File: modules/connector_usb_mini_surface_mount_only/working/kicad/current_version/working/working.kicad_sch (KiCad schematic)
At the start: 1 part, among them J1 scumnsmo

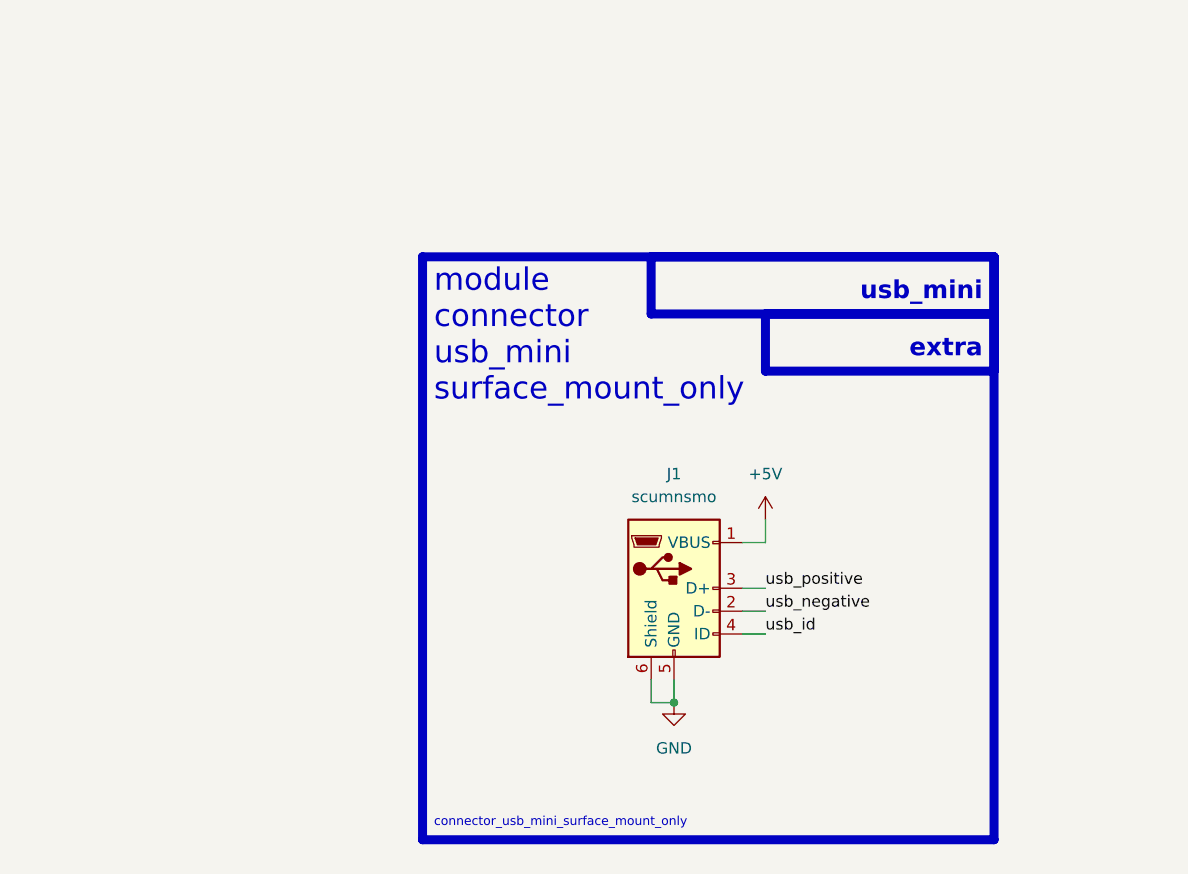
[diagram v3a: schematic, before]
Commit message: schematic formatting
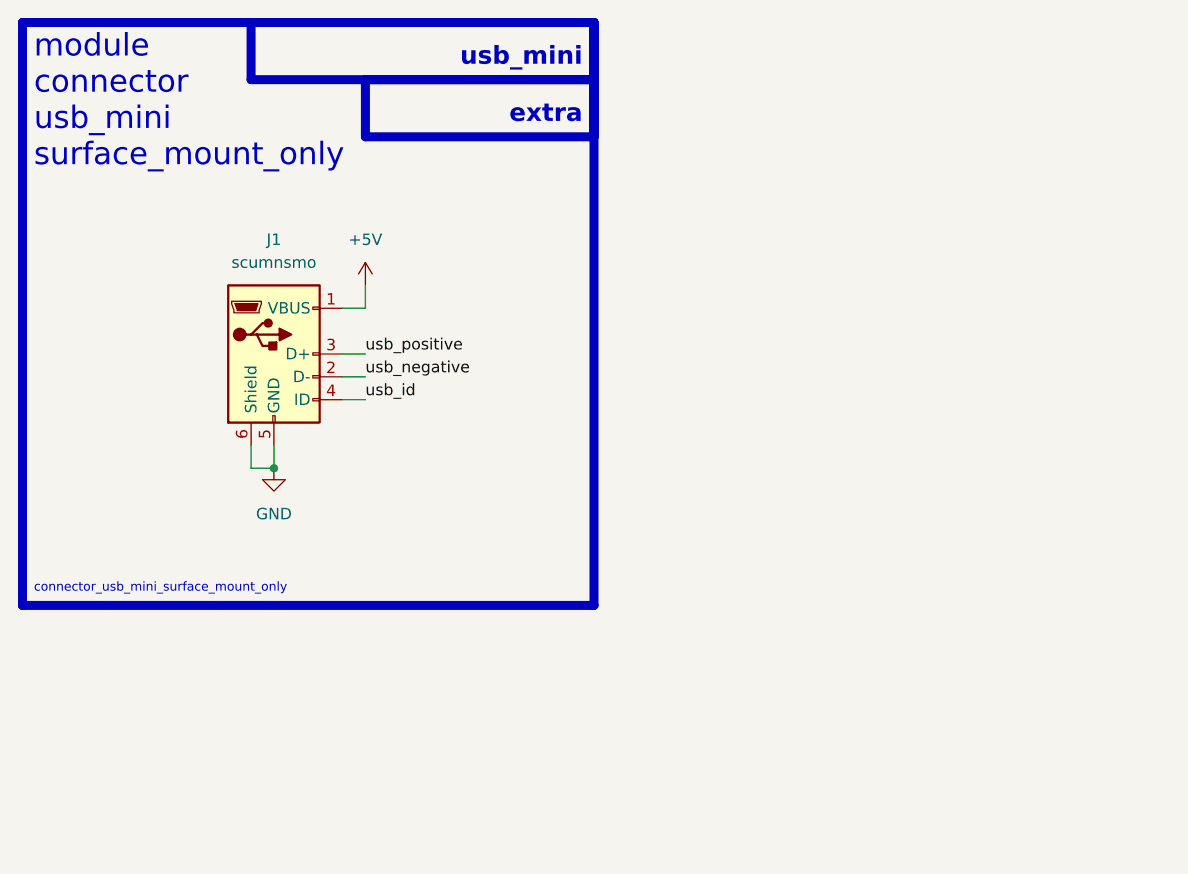
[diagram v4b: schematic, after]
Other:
- moved on the sheet: J1
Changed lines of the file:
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@@
 (kicad_sch (version 20230121) (generator eeschema)
-  (paper "A4")
-  (junction (at 146.05 110.49) (diameter 0) (color 0 0 0 0)
+  (paper "A5")
+  (junction (at 101.6 84.455) (diameter 0) (color 0 0 0 0)
   )
-  (wire (pts (xy 153.67 102.87) (xy 156.21 102.87))
+  (wire (pts (xy 109.22 76.835) (xy 111.76 76.835))
     (stroke (width 0) (type default))
   )
-  (wire (pts (xy 146.05 107.95) (xy 146.05 110.49))
+  (wire (pts (xy 101.6 81.915) (xy 101.6 84.455))
     (stroke (width 0) (type default))
   )
-  (wire (pts (xy 156.21 90.17) (xy 156.21 92.71))
+  (wire (pts (xy 111.76 64.135) (xy 111.76 66.675))
     (stroke (width 0) (type default))
   )
-  (wire (pts (xy 153.67 97.79) (xy 156.21 97.79))
+  (wire (pts (xy 109.22 71.755) (xy 111.76 71.755))
     (stroke (width 0) (type default))
   )
-  (wire (pts (xy 143.51 110.49) (xy 146.05 110.49))
+  (wire (pts (xy 99.06 84.455) (xy 101.6 84.455))
     (stroke (width 0) (type default))
   )
-  (wire (pts (xy 153.67 92.71) (xy 156.21 92.71))
+  (wire (pts (xy 109.22 66.675) (xy 111.76 66.675))
     (stroke (width 0) (type default))
   )
-  (wire (pts (xy 143.51 107.95) (xy 143.51 110.49))
+  (wire (pts (xy 99.06 81.915) (xy 99.06 84.455))
     (stroke (width 0) (type default))
   )
-  (wire (pts (xy 153.67 100.33) (xy 156.21 100.33))
+  (wire (pts (xy 109.22 74.295) (xy 111.76 74.295))
     (stroke (width 0) (type default))
   )
-  (rectangle (start 118.11 60.96) (end 181.61 125.73)
+  (rectangle (start 73.66 34.925) (end 137.16 99.695)
     (stroke (width 1) (type default))
     (fill (type none))
   )
-  (rectangle (start 156.21 67.31) (end 181.61 73.66)
+  (rectangle (start 111.76 41.275) (end 137.16 47.625)
     (stroke (width 1) (type default))
     (fill (type none))
   )
-  (rectangle (start 143.51 60.96) (end 181.61 67.31)
+  (rectangle (start 99.06 34.925) (end 137.16 41.275)
     (stroke (width 1) (type default))
     (fill (type none))
   )
-  (text "extra" (at 180.34 72.39 0)
+  (text "extra" (at 135.89 46.355 0)
     (effects (font (size 2 2) (thickness 0.8) bold) (justify right bottom))
   )
-  (text "usb_mini" (at 180.34 66.04 0)
+  (text "usb_mini" (at 135.89 40.005 0)
     (effects (font (size 2 2) (thickness 0.8) bold) (justify right bottom))
   )
-  (text "module\nconnector\nusb_mini\nsurface_mount_only\n\n" (at 119.38 81.28 0)
+  (text "module\nconnector\nusb_mini\nsurface_mount_only\n\n" (at 74.93 55.245 0)
     (effects (font (size 2.5 2.5)) (justify left bottom))
   )
-  (text "connector_usb_mini_surface_mount_only" (at 119.38 124.46 0)
+  (text "connector_usb_mini_surface_mount_only" (at 74.93 98.425 0)
     (effects (font (size 1 1)) (justify left bottom))
   )
-  (label "usb_id" (at 156.21 102.87 0) (fields_autoplaced)
+  (label "usb_id" (at 111.76 76.835 0) (fields_autoplaced)
     (effects (font (size 1.27 1.27)) (justify left bottom))
   )
-  (label "usb_positive" (at 156.21 97.79 0) (fields_autoplaced)
+  (label "usb_positive" (at 111.76 71.755 0) (fields_autoplaced)
     (effects (font (size 1.27 1.27)) (justify left bottom))
   )
-  (label "usb_negative" (at 156.21 100.33 0) (fields_autoplaced)
+  (label "usb_negative" (at 111.76 74.295 0) (fields_autoplaced)
     (effects (font (size 1.27 1.27)) (justify left bottom))
   )
-  (symbol (lib_id "power:GND") (at 146.05 110.49 0) (unit 1)
+  (symbol (lib_id "power:GND") (at 101.6 84.455 0) (unit 1)
     (in_bom yes) (on_board yes) (dnp no) (fields_autoplaced)
-    (property "Reference" "#PWR012" (at 146.05 116.84 0)
+    (property "Reference" "#PWR012" (at 101.6 90.805 0)
       (effects (font (size 1.27 1.27)) hide)
     )
-    (property "Value" "GND" (at 146.05 115.57 0)
+    (property "Value" "GND" (at 101.6 89.535 0)
       (effects (font (size 1.27 1.27)))
     )
-    (property "Footprint" "" (at 146.05 110.49 0)
+    (property "Footprint" "" (at 101.6 84.455 0)
       (effects (font (size 1.27 1.27)) hide)
     )
-    (property "Datasheet" "" (at 146.05 110.49 0)
+    (property "Datasheet" "" (at 101.6 84.455 0)
       (effects (font (size 1.27 1.27)) hide)
     )
@@
     )
   )
-  (symbol (lib_id "power:+5V") (at 156.21 90.17 0) (unit 1)
+  (symbol (lib_id "power:+5V") (at 111.76 64.135 0) (unit 1)
     (in_bom yes) (on_board yes) (dnp no) (fields_autoplaced)
-    (property "Reference" "#PWR013" (at 156.21 93.98 0)
+    (property "Reference" "#PWR013" (at 111.76 67.945 0)
       (effects (font (size 1.27 1.27)) hide)
     )
-    (property "Value" "+5V" (at 156.21 85.09 0)
+    (property "Value" "+5V" (at 111.76 59.055 0)
       (effects (font (size 1.27 1.27)))
     )
-    (property "Footprint" "" (at 156.21 90.17 0)
+    (property "Footprint" "" (at 111.76 64.135 0)
       (effects (font (size 1.27 1.27)) hide)
     )
-    (property "Datasheet" "" (at 156.21 90.17 0)
+    (property "Datasheet" "" (at 111.76 64.135 0)
       (effects (font (size 1.27 1.27)) hide)
     )
@@
     )
   )
-  (symbol (lib_id "oomlout_oomp_part_symbols:scumnsmo_electronic_socket_usb_mini_surface_mount_only") (at 146.05 97.79 0) (unit 1)
+  (symbol (lib_id "oomlout_oomp_part_symbols:scumnsmo_electronic_socket_usb_mini_surface_mount_only") (at 101.6 71.755 0) (unit 1)
     (in_bom yes) (on_board yes) (dnp no) (fields_autoplaced)
-    (property "Reference" "J1" (at 146.05 85.09 0)
+    (property "Reference" "J1" (at 101.6 59.055 0)
       (effects (font (size 1.27 1.27)))
     )
-    (property "Value" "scumnsmo" (at 146.05 87.63 0)
+    (property "Value" "scumnsmo" (at 101.6 61.595 0)
       (effects (font (size 1.27 1.27)))
     )
-    (property "Footprint" "oomlout_oomp_part_footprints:scumnsmo_electronic_socket_usb_mini_surface_mount_only" (at 149.86 99.06 0)
+    (property "Footprint" "oomlout_oomp_part_footprints:scumnsmo_electronic_socket_usb_mini_surface_mount_only" (at 105.41 73.025 0)
       (effects (font (size 1.27 1.27)) hide)
     )
-    (property "Datasheet" "https://github.com/oomlout/oomlout_oomp_v3/parts/electronic_socket_usb_mini_surface_mount_only/datasheet.pdf" (at 149.86 99.06 0)
+    (property "Datasheet" "https://github.com/oomlout/oomlout_oomp_v3/parts/electronic_socket_usb_mini_surface_mount_only/datasheet.pdf" (at 105.41 73.025 0)
       (effects (font (size 1.27 1.27)) hide)
     )
